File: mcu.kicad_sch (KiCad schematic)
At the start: 47 parts, among them J1 USB_B, J2 Conn_01x05_Pin, SW1 SW_Push, U1 STM32F103CBTx, U2 USB6B1, U3 AMS1117-3.3, Y1 8Mhz

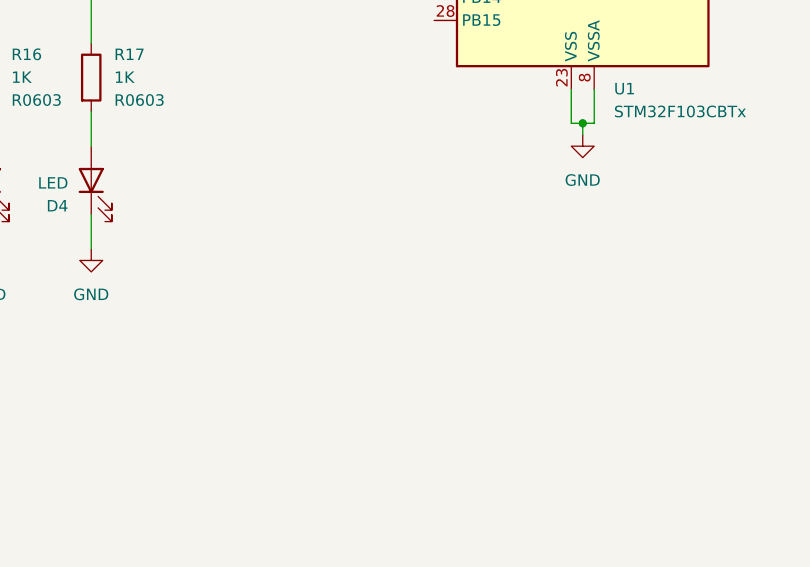
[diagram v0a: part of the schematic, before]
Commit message: pcb components relocated.
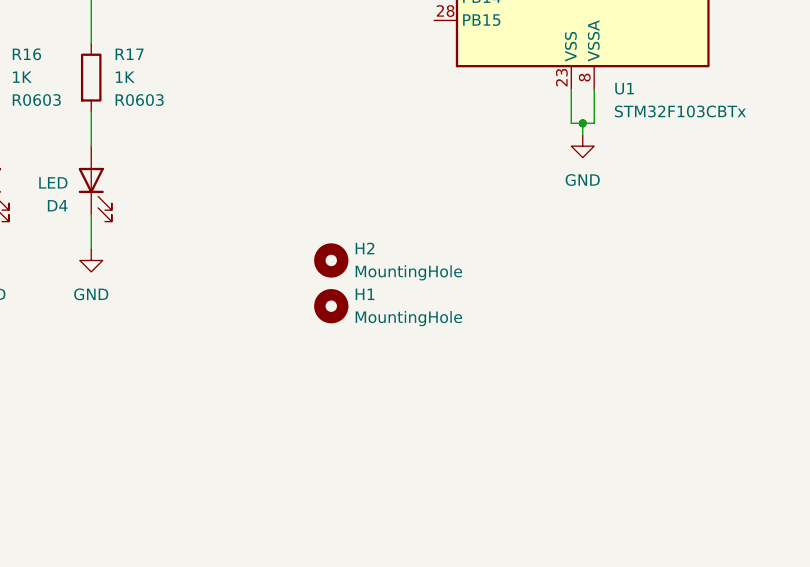
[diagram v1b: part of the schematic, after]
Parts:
- added H1, H2: MountingHole, MountingHole:MountingHole_3mm_Pad_Via, symbol Mechanical:MountingHole
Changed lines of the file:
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@@
+	)
+	(symbol
+		(lib_id "Mechanical:MountingHole")
+		(at 200.66 156.21 0)
+		(unit 1)
+		(exclude_from_sim yes)
+		(in_bom no)
+		(on_board yes)
+		(dnp no)
+		(fields_autoplaced yes)
+		(property "Reference" "H1"
+			(at 203.2 154.9399 0)
+			(effects
+				(font
+					(size 1.27 1.27)
+				)
+				(justify left)
+			)
+		)
+		(property "Value" "MountingHole"
+			(at 203.2 157.4799 0)
+			(effects
+				(font
+					(size 1.27 1.27)
+				)
+				(justify left)
+			)
+		)
+		(property "Footprint" "MountingHole:MountingHole_3mm_Pad_Via"
+			(at 200.66 156.21 0)
+			(effects
+				(font
+					(size 1.27 1.27)
+				)
+				(hide yes)
+			)
+		)
+		(property "Datasheet" "~"
+			(at 200.66 156.21 0)
+			(effects
+				(font
+					(size 1.27 1.27)
+				)
+				(hide yes)
+			)
+		)
+		(property "Description" "Mounting Hole without connection"
+			(at 200.66 156.21 0)
+			(effects
+				(font
+					(size 1.27 1.27)
+				)
+				(hide yes)
+			)
+		)
+		(instances
+			(project ""
+				(path "/c46f0577-8378-47ed-a184-c512ebaa7448/cf4a56a0-87cc-48b2-b91a-72f3bf53d7c4"
+					(reference "H1")
+					(unit 1)
+				)
+			)
+		)
 	)
 	(symbol
@@
 					(unit 1)
 				)
+			)
+		)
+	)
+	(symbol
+		(lib_id "Mechanical:MountingHole")
+		(at 200.66 151.13 0)
+		(unit 1)
+		(exclude_from_sim yes)
+		(in_bom no)
+		(on_board yes)
+		(dnp no)
+		(fields_autoplaced yes)
+		(property "Reference" "H2"
+			(at 203.2 149.8599 0)
+			(effects
+				(font
+					(size 1.27 1.27)
+				)
+				(justify left)
+			)
+		)
+		(property "Value" "MountingHole"
+			(at 203.2 152.3999 0)
+			(effects
+				(font
+					(size 1.27 1.27)
+				)
+				(justify left)
+			)
+		)
+		(property "Footprint" "MountingHole:MountingHole_3mm_Pad_Via"
+			(at 200.66 151.13 0)
+			(effects
+				(font
+					(size 1.27 1.27)
+				)
+				(hide yes)
+			)
+		)
+		(property "Datasheet" "~"
+			(at 200.66 151.13 0)
+			(effects
+				(font
+					(size 1.27 1.27)
+				)
+				(hide yes)
+			)
+		)
+		(property "Description" "Mounting Hole without connection"
+			(at 200.66 151.13 0)
+			(effects
+				(font
+					(size 1.27 1.27)
+				)
+				(hide yes)
+			)
+		)
+		(instances
+			(project "bmp_x6"
+				(path "/c46f0577-8378-47ed-a184-c512ebaa7448/cf4a56a0-87cc-48b2-b91a-72f3bf53d7c4"
+					(reference "H2")
+					(unit 1)
+				)

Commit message: shorcuts updated and components relocated.
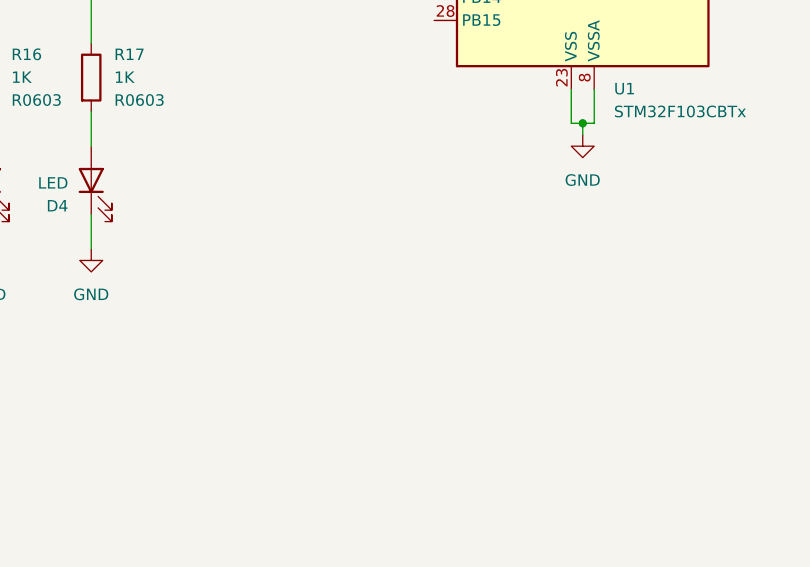
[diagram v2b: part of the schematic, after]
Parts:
- removed H1, H2: MountingHole, MountingHole:MountingHole_3mm_Pad_Via, symbol Mechanical:MountingHole
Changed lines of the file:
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@@
-	)
-	(symbol
-		(lib_id "Mechanical:MountingHole")
-		(at 200.66 156.21 0)
-		(unit 1)
-		(exclude_from_sim yes)
-		(in_bom no)
-		(on_board yes)
-		(dnp no)
-		(fields_autoplaced yes)
-		(property "Reference" "H1"
-			(at 203.2 154.9399 0)
-			(effects
-				(font
-					(size 1.27 1.27)
-				)
-				(justify left)
-			)
-		)
-		(property "Value" "MountingHole"
-			(at 203.2 157.4799 0)
-			(effects
-				(font
-					(size 1.27 1.27)
-				)
-				(justify left)
-			)
-		)
-		(property "Footprint" "MountingHole:MountingHole_3mm_Pad_Via"
-			(at 200.66 156.21 0)
-			(effects
-				(font
-					(size 1.27 1.27)
-				)
-				(hide yes)
-			)
-		)
-		(property "Datasheet" "~"
-			(at 200.66 156.21 0)
-			(effects
-				(font
-					(size 1.27 1.27)
-				)
-				(hide yes)
-			)
-		)
-		(property "Description" "Mounting Hole without connection"
-			(at 200.66 156.21 0)
-			(effects
-				(font
-					(size 1.27 1.27)
-				)
-				(hide yes)
-			)
-		)
-		(instances
-			(project ""
-				(path "/c46f0577-8378-47ed-a184-c512ebaa7448/cf4a56a0-87cc-48b2-b91a-72f3bf53d7c4"
-					(reference "H1")
-					(unit 1)
-				)
-			)
-		)
 	)
 	(symbol
@@
 					(unit 1)
 				)
-			)
-		)
-	)
-	(symbol
-		(lib_id "Mechanical:MountingHole")
-		(at 200.66 151.13 0)
-		(unit 1)
-		(exclude_from_sim yes)
-		(in_bom no)
-		(on_board yes)
-		(dnp no)
-		(fields_autoplaced yes)
-		(property "Reference" "H2"
-			(at 203.2 149.8599 0)
-			(effects
-				(font
-					(size 1.27 1.27)
-				)
-				(justify left)
-			)
-		)
-		(property "Value" "MountingHole"
-			(at 203.2 152.3999 0)
-			(effects
-				(font
-					(size 1.27 1.27)
-				)
-				(justify left)
-			)
-		)
-		(property "Footprint" "MountingHole:MountingHole_3mm_Pad_Via"
-			(at 200.66 151.13 0)
-			(effects
-				(font
-					(size 1.27 1.27)
-				)
-				(hide yes)
-			)
-		)
-		(property "Datasheet" "~"
-			(at 200.66 151.13 0)
-			(effects
-				(font
-					(size 1.27 1.27)
-				)
-				(hide yes)
-			)
-		)
-		(property "Description" "Mounting Hole without connection"
-			(at 200.66 151.13 0)
-			(effects
-				(font
-					(size 1.27 1.27)
-				)
-				(hide yes)
-			)
-		)
-		(instances
-			(project "bmp_x6"
-				(path "/c46f0577-8378-47ed-a184-c512ebaa7448/cf4a56a0-87cc-48b2-b91a-72f3bf53d7c4"
-					(reference "H2")
-					(unit 1)
-				)
